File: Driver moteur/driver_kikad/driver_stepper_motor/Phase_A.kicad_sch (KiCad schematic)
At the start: 19 parts

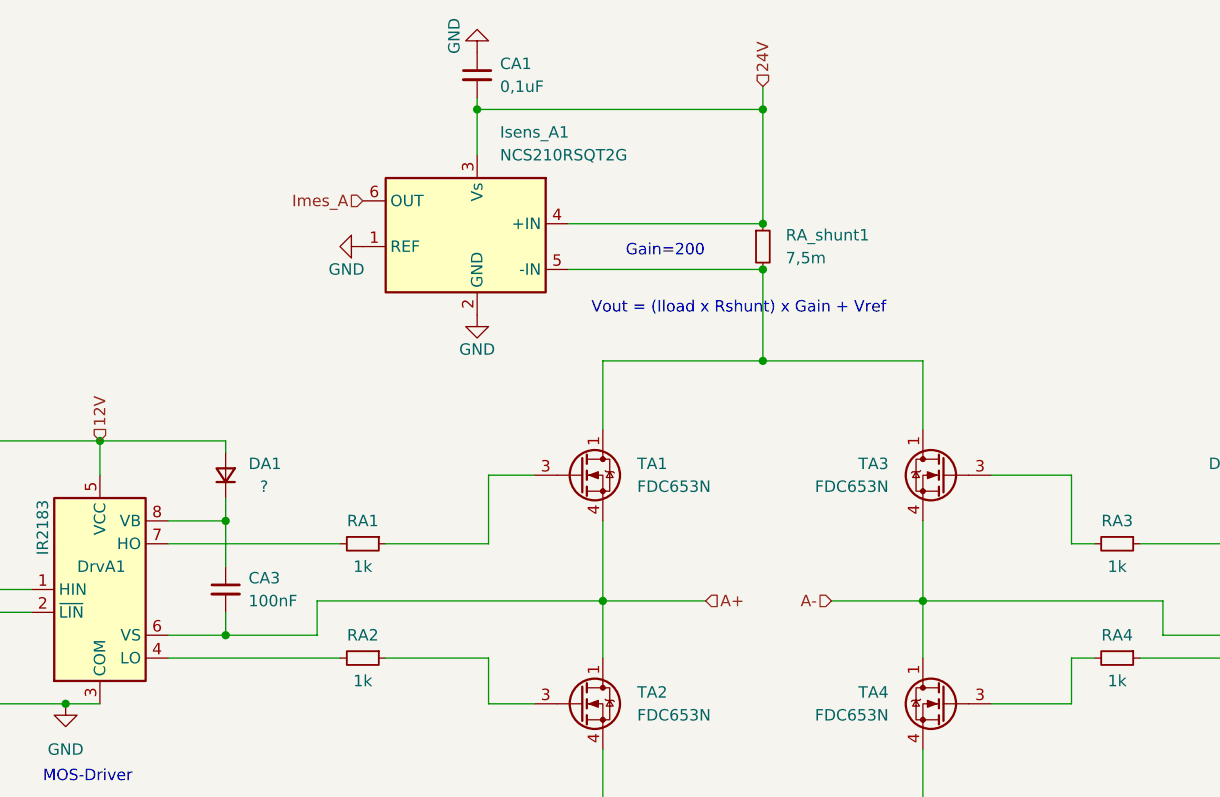
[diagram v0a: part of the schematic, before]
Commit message: Driver modifié avec les bonnes valeurs et les bonnes datasheet
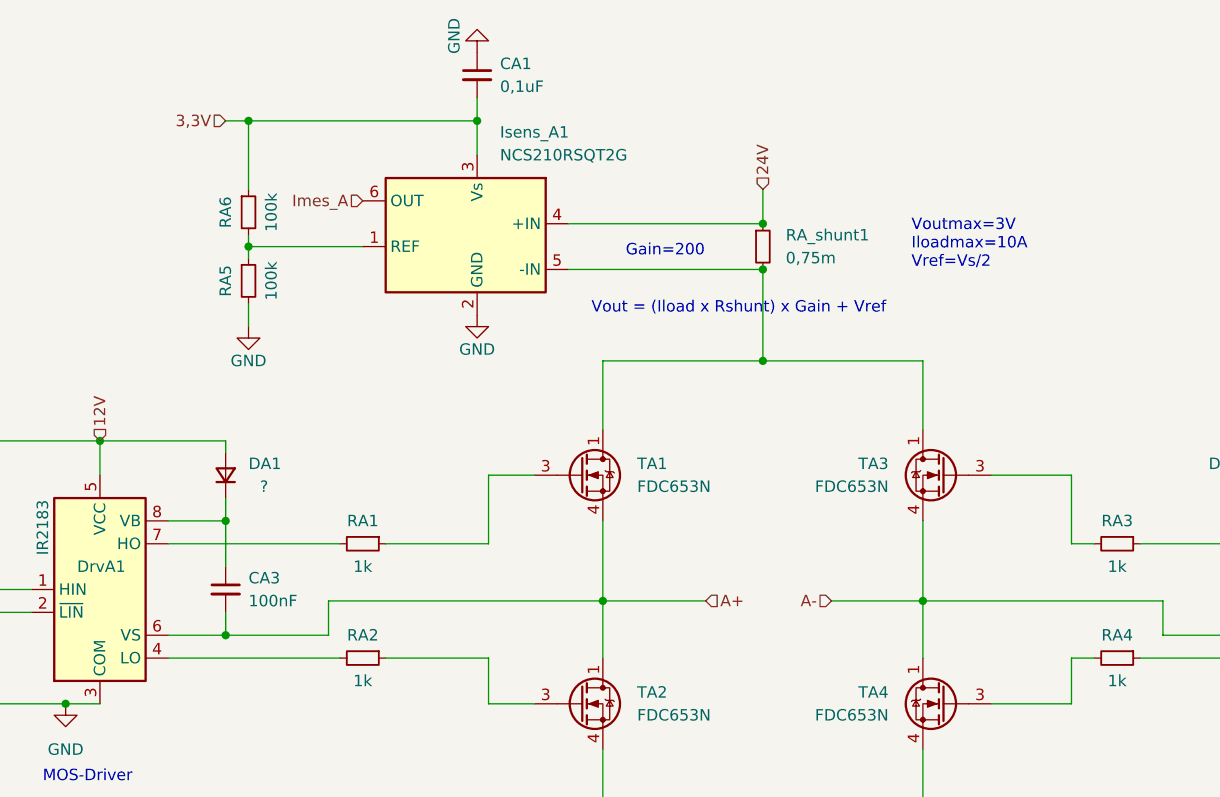
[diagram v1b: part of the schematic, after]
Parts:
- added RA5, RA6: 100k, Resistor_SMD:R_0603_1608Metric, symbol Device:R_Small
- RA_shunt1: value 7,5m -> 0,75m
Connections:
- net 24V: no longer CA1.2, Isens_A1.3 (Vs)
- net GND: now also RA5.2; no longer Isens_A1.1 (REF)
- new net: Isens_A1.1 (REF), RA5.1, RA6.2
- new net 3,3V: CA1.2, Isens_A1.3 (Vs), RA6.1
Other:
- note added: "Voutmax=3V Iloadmax=10A Vref=Vs/2"
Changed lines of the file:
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@@
     (company "Tom CHARBONNEAU")
   )
-  (junction (at 152.4 38.1) (diameter 0) (color 0 0 0 0)
-  )
   (junction (at 74.93 104.14) (diameter 0) (color 0 0 0 0)
   )
+  (junction (at 120.65 39.37) (diameter 0) (color 0 0 0 0)
+  )
   (junction (at 92.71 83.82) (diameter 0) (color 0 0 0 0)
   )
@@
   (junction (at 152.4 66.04) (diameter 0) (color 0 0 0 0)
   )
-  (junction (at 120.65 38.1) (diameter 0) (color 0 0 0 0)
+  (junction (at 95.25 39.37) (diameter 0) (color 0 0 0 0)
   )
   (junction (at 134.62 92.71) (diameter 0) (color 0 0 0 0)
@@
   (junction (at 152.4 115.57) (diameter 0) (color 0 0 0 0)
   )
+  (junction (at 95.25 53.34) (diameter 0) (color 0 0 0 0)
+  )
   (junction (at 78.74 74.93) (diameter 0) (color 0 0 0 0)
   )
@@
     (stroke (width 0) (type default) (color 0 0 0 0))
   )
-  (wire (pts (xy 120.65 38.1) (xy 152.4 38.1))
-    (stroke (width 0) (type default) (color 0 0 0 0))
-  )
   (wire (pts (xy 110.49 86.36) (xy 121.92 86.36))
     (stroke (width 0) (type default) (color 0 0 0 0))
@@
     (stroke (width 0) (type default) (color 0 0 0 0))
   )
-  (wire (pts (xy 92.71 96.52) (xy 102.87 96.52))
+  (wire (pts (xy 95.25 52.07) (xy 95.25 53.34))
+    (stroke (width 0) (type default) (color 0 0 0 0))
+  )
+  (wire (pts (xy 92.71 96.52) (xy 104.14 96.52))
     (stroke (width 0) (type default) (color 0 0 0 0))
   )
@@
     (stroke (width 0) (type default) (color 0 0 0 0))
   )
-  (wire (pts (xy 102.87 96.52) (xy 102.87 92.71))
+  (wire (pts (xy 104.14 96.52) (xy 104.14 92.71))
+    (stroke (width 0) (type default) (color 0 0 0 0))
+  )
+  (wire (pts (xy 120.65 39.37) (xy 120.65 43.18))
     (stroke (width 0) (type default) (color 0 0 0 0))
   )
@@
     (stroke (width 0) (type default) (color 0 0 0 0))
   )
+  (wire (pts (xy 92.71 39.37) (xy 95.25 39.37))
+    (stroke (width 0) (type default) (color 0 0 0 0))
+  )
   (wire (pts (xy 92.71 83.82) (xy 92.71 88.9))
     (stroke (width 0) (type default) (color 0 0 0 0))
@@
     (stroke (width 0) (type default) (color 0 0 0 0))
   )
-  (wire (pts (xy 120.65 38.1) (xy 120.65 43.18))
+  (wire (pts (xy 120.65 36.83) (xy 120.65 39.37))
     (stroke (width 0) (type default) (color 0 0 0 0))
   )
@@
     (stroke (width 0) (type default) (color 0 0 0 0))
   )
-  (wire (pts (xy 152.4 35.56) (xy 152.4 38.1))
+  (wire (pts (xy 152.4 46.99) (xy 152.4 50.8))
     (stroke (width 0) (type default) (color 0 0 0 0))
   )
@@
     (stroke (width 0) (type default) (color 0 0 0 0))
   )
+  (wire (pts (xy 95.25 53.34) (xy 107.95 53.34))
+    (stroke (width 0) (type default) (color 0 0 0 0))
+  )
   (wire (pts (xy 92.71 74.93) (xy 78.74 74.93))
     (stroke (width 0) (type default) (color 0 0 0 0))
@@
     (stroke (width 0) (type default) (color 0 0 0 0))
   )
+  (wire (pts (xy 95.25 39.37) (xy 120.65 39.37))
+    (stroke (width 0) (type default) (color 0 0 0 0))
+  )
   (wire (pts (xy 170.18 66.04) (xy 170.18 73.66))
     (stroke (width 0) (type default) (color 0 0 0 0))
   )
+  (wire (pts (xy 95.25 59.69) (xy 95.25 62.23))
+    (stroke (width 0) (type default) (color 0 0 0 0))
+  )
   (wire (pts (xy 170.18 92.71) (xy 196.85 92.71))
     (stroke (width 0) (type default) (color 0 0 0 0))
@@
     (stroke (width 0) (type default) (color 0 0 0 0))
   )
-  (wire (pts (xy 152.4 38.1) (xy 152.4 50.8))
-    (stroke (width 0) (type default) (color 0 0 0 0))
-  )
   (wire (pts (xy 130.81 50.8) (xy 152.4 50.8))
     (stroke (width 0) (type default) (color 0 0 0 0))
@@
     (stroke (width 0) (type default) (color 0 0 0 0))
   )
-  (wire (pts (xy 120.65 36.83) (xy 120.65 38.1))
-    (stroke (width 0) (type default) (color 0 0 0 0))
-  )
   (wire (pts (xy 64.77 81.28) (xy 64.77 74.93))
     (stroke (width 0) (type default) (color 0 0 0 0))
@@
     (stroke (width 0) (type default) (color 0 0 0 0))
   )
+  (wire (pts (xy 95.25 53.34) (xy 95.25 54.61))
+    (stroke (width 0) (type default) (color 0 0 0 0))
+  )
   (wire (pts (xy 64.77 74.93) (xy 78.74 74.93))
     (stroke (width 0) (type default) (color 0 0 0 0))
@@
     (stroke (width 0) (type default) (color 0 0 0 0))
   )
-  (wire (pts (xy 102.87 92.71) (xy 134.62 92.71))
+  (wire (pts (xy 104.14 92.71) (xy 134.62 92.71))
     (stroke (width 0) (type default) (color 0 0 0 0))
   )
@@
   )
   (wire (pts (xy 110.49 99.06) (xy 121.92 99.06))
+    (stroke (width 0) (type default) (color 0 0 0 0))
+  )
+  (wire (pts (xy 95.25 39.37) (xy 95.25 46.99))
     (stroke (width 0) (type default) (color 0 0 0 0))
   )
@@
   )
   (text "Vout = (Iload x Rshunt) x Gain + Vref" (at 133.35 60.96 0)
+    (effects (font (size 1.27 1.27)) (justify left bottom))
+  )
+  (text "Voutmax=3V\nIloadmax=10A\nVref=Vs/2" (at 168.91 55.88 0)
     (effects (font (size 1.27 1.27)) (justify left bottom))
   )
@@
     (effects (font (size 1.27 1.27)) (justify right))
   )
-  (hierarchical_label "24V" (shape input) (at 152.4 35.56 90)
+  (hierarchical_label "3,3V" (shape input) (at 92.71 39.37 180)
+    (effects (font (size 1.27 1.27)) (justify right))
+  )
+  (hierarchical_label "24V" (shape input) (at 152.4 46.99 90)
     (effects (font (size 1.27 1.27)) (justify left))
   )
@@
     (pin "2")
   )
+  (symbol (lib_id "Device:R_Small") (at 95.25 49.53 0) (unit 1)
+    (in_bom yes) (on_board yes)
+    (property "Reference" "RA6" (id 0) (at 92.71 49.53 90))
+    (property "Value" "100k" (id 1) (at 97.79 49.53 90))
+    (property "Footprint" "Resistor_SMD:R_0603_1608Metric" (id 2) (at 95.25 49.53 0)
+      (effects (font (size 1.27 1.27)) hide)
+    )
+    (property "Datasheet" "~" (id 3) (at 95.25 49.53 0)
+      (effects (font (size 1.27 1.27)) hide)
+    )
+    (pin "1")
+    (pin "2")
+  )
+  (symbol (lib_id "power:GND") (at 95.25 62.23 0) (unit 1)
+    (in_bom yes) (on_board yes)
+    (property "Reference" "#PWR?" (id 0) (at 95.25 68.58 0)
+      (effects (font (size 1.27 1.27)) hide)
+    )
+    (property "Value" "GND" (id 1) (at 95.25 66.04 0))
+    (property "Footprint" "" (id 2) (at 95.25 62.23 0)
+      (effects (font (size 1.27 1.27)) hide)
+    )
+    (property "Datasheet" "" (id 3) (at 95.25 62.23 0)
+      (effects (font (size 1.27 1.27)) hide)
+    )
+    (pin "1")
+  )
   (symbol (lib_id "Device:C_Small") (at 120.65 34.29 0) (unit 1)
     (in_bom yes) (on_board yes) (fields_autoplaced)
@@
     )
     (property "Datasheet" "" (id 3) (at 152.4 118.11 0)
-      (effects (font (size 1.27 1.27)) hide)
-    )
-    (pin "1")
-  )
-  (symbol (lib_id "power:GND") (at 107.95 53.34 270) (unit 1)
-    (in_bom yes) (on_board yes)
-    (property "Reference" "#PWR0101" (id 0) (at 101.6 53.34 0)
-      (effects (font (size 1.27 1.27)) hide)
-    )
-    (property "Value" "GND" (id 1) (at 104.14 55.88 90)
-      (effects (font (size 1.27 1.27)) (justify left))
-    )
-    (property "Footprint" "" (id 2) (at 107.95 53.34 0)
-      (effects (font (size 1.27 1.27)) hide)
-    )
-    (property "Datasheet" "" (id 3) (at 107.95 53.34 0)
       (effects (font (size 1.27 1.27)) hide)
     )
@@
       (effects (font (size 1.27 1.27)) (justify left))
     )
-    (property "Value" "7,5m" (id 1) (at 154.94 54.6099 0)
+    (property "Value" "0,75m" (id 1) (at 154.94 54.6099 0)
       (effects (font (size 1.27 1.27)) (justify left))
     )
@@
     (pin "8")
   )
+  (symbol (lib_id "Device:R_Small") (at 95.25 57.15 0) (unit 1)
+    (in_bom yes) (on_board yes)
+    (property "Reference" "RA5" (id 0) (at 92.71 57.15 90))
+    (property "Value" "100k" (id 1) (at 97.79 57.15 90))
+    (property "Footprint" "Resistor_SMD:R_0603_1608Metric" (id 2) (at 95.25 57.15 0)
+      (effects (font (size 1.27 1.27)) hide)
+    )
+    (property "Datasheet" "~" (id 3) (at 95.25 57.15 0)
+      (effects (font (size 1.27 1.27)) hide)
+    )
+    (pin "1")
+    (pin "2")
+  )
   (symbol (lib_id "Transistor_FET:FDC2512") (at 172.72 104.14 0) (mirror y) (unit 1)

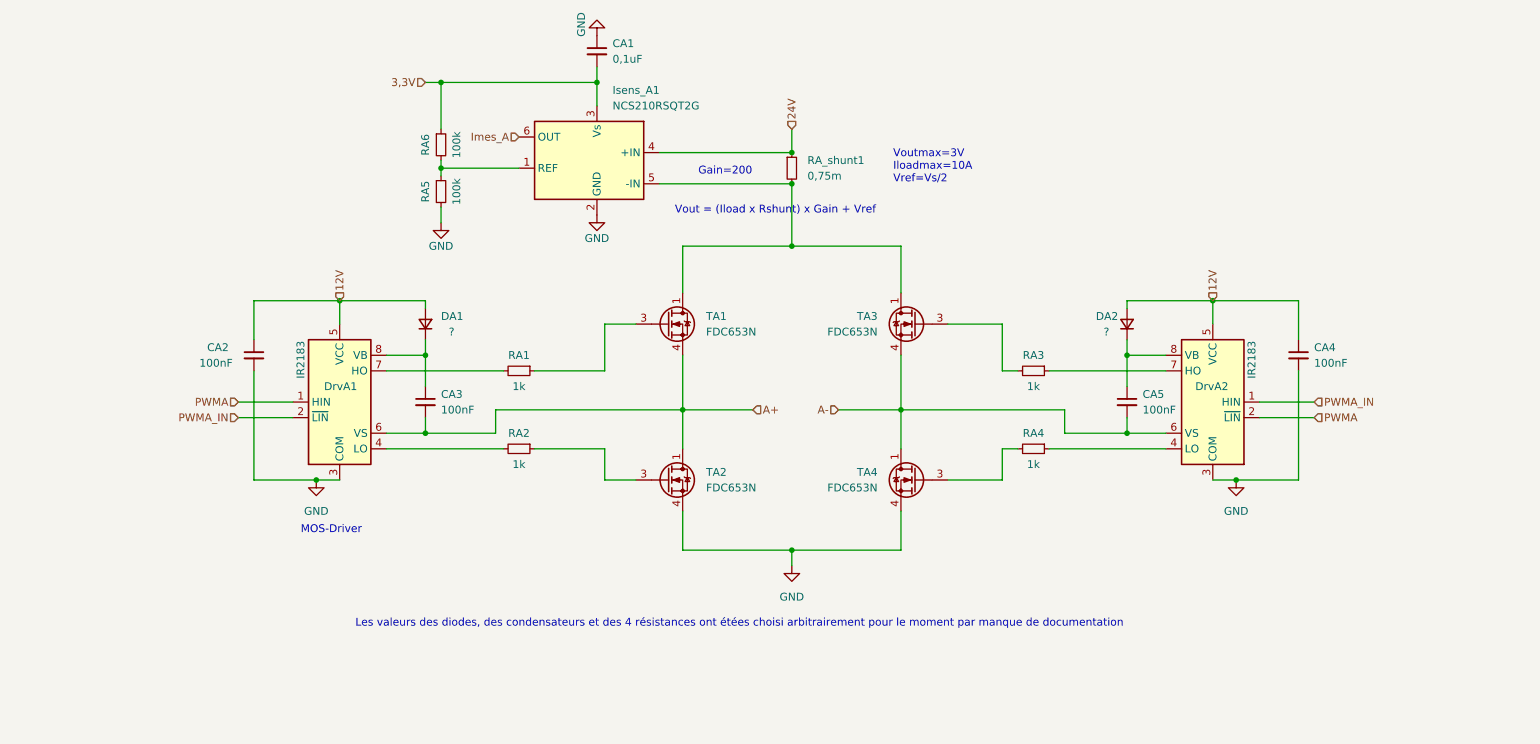
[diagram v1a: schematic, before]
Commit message: PCB root sans erreurs
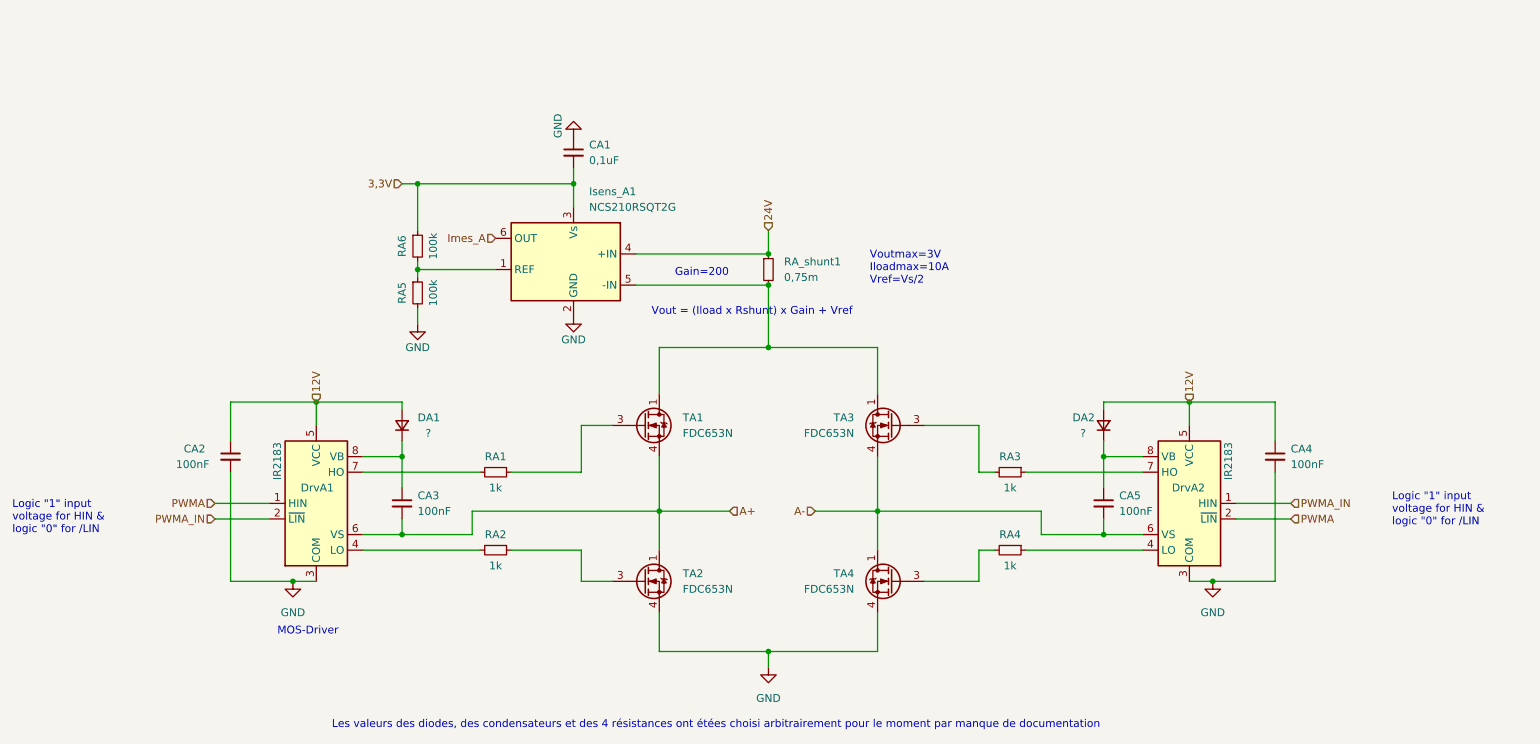
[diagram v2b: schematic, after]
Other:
- note added: "Logic "1" input voltage for HIN & logic "0" for /LIN"
- moved on the sheet: CA1, CA2, CA3, CA4, CA5, DA1, DA2, DrvA1, DrvA2, Isens_A1, RA1, RA2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
